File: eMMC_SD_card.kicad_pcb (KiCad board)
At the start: 4 copper layers, 24 x 20.3 mm, 29 parts, among them J1 SD_Card, U1 eMMC_5.1_BGA153

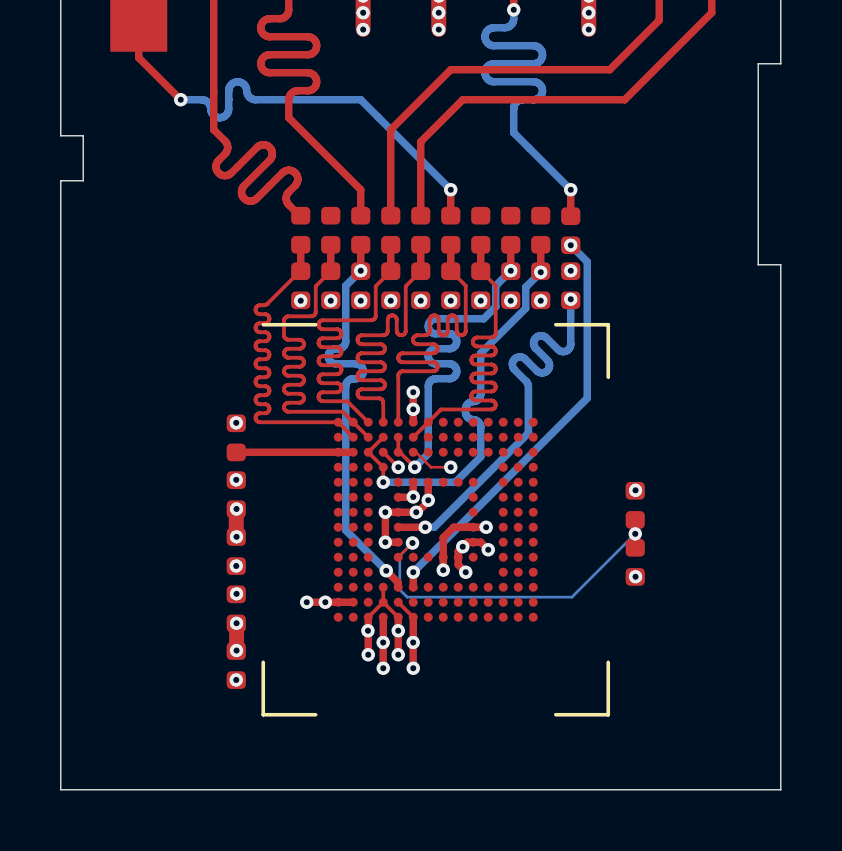
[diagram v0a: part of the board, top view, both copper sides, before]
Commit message: Introduce separate VCC and VCCq domains
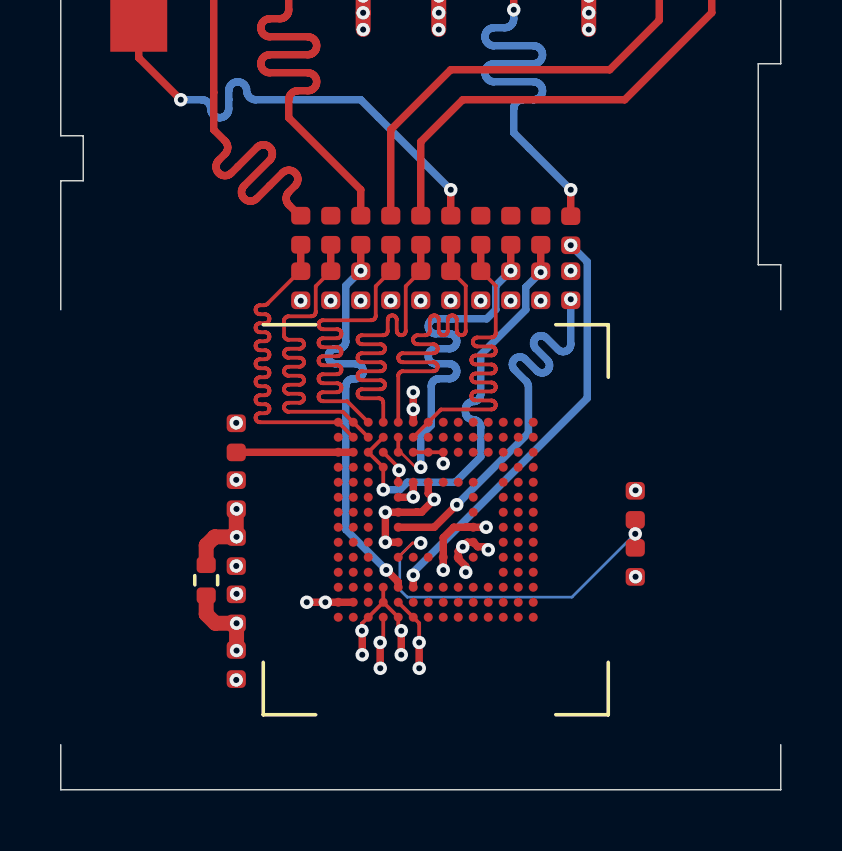
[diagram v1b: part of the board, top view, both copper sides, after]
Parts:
- added R22: 0R, Resistor_SMD:R_0402_1005Metric, F.Cu at (104.8, 125.0)
- moved C4 3.80 mm to (105.8, 124.1)
- moved C5 3.77 mm to (105.8, 127.8)
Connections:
- C5 pad 1: VCC -> VCCQ
- C6 pad 1: VCC -> VCCQ
- U1 pad C1: Net-(C2-Pad1) -> (no net)
- U1 pad C6: VCC -> VCCQ
- U1 pad C7: (no net) -> VCCQ
- U1 pad C8: (no net) -> VCCQ
- U1 pad M4: VCC -> VCCQ
- U1 pad N1: GND -> (no net)
- U1 pad N4: VCC -> VCCQ
- U1 pad P3: VCC -> VCCQ
- U1 pad P5: VCC -> VCCQ
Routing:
- net VCCQ: track 0.00 -> 8.67 mm, vias 0 -> 7
- net VCC: track 14.3 -> 9.29 mm, vias 26 -> 19
- net GND: track 21.1 -> 22.0 mm, vias 28 -> 27
- net Net-(C1-Pad2): track 12.2 -> 12.7 mm
- added copper zone on VCC, net VCCQ
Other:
- outline, holes or cut-outs redrawn

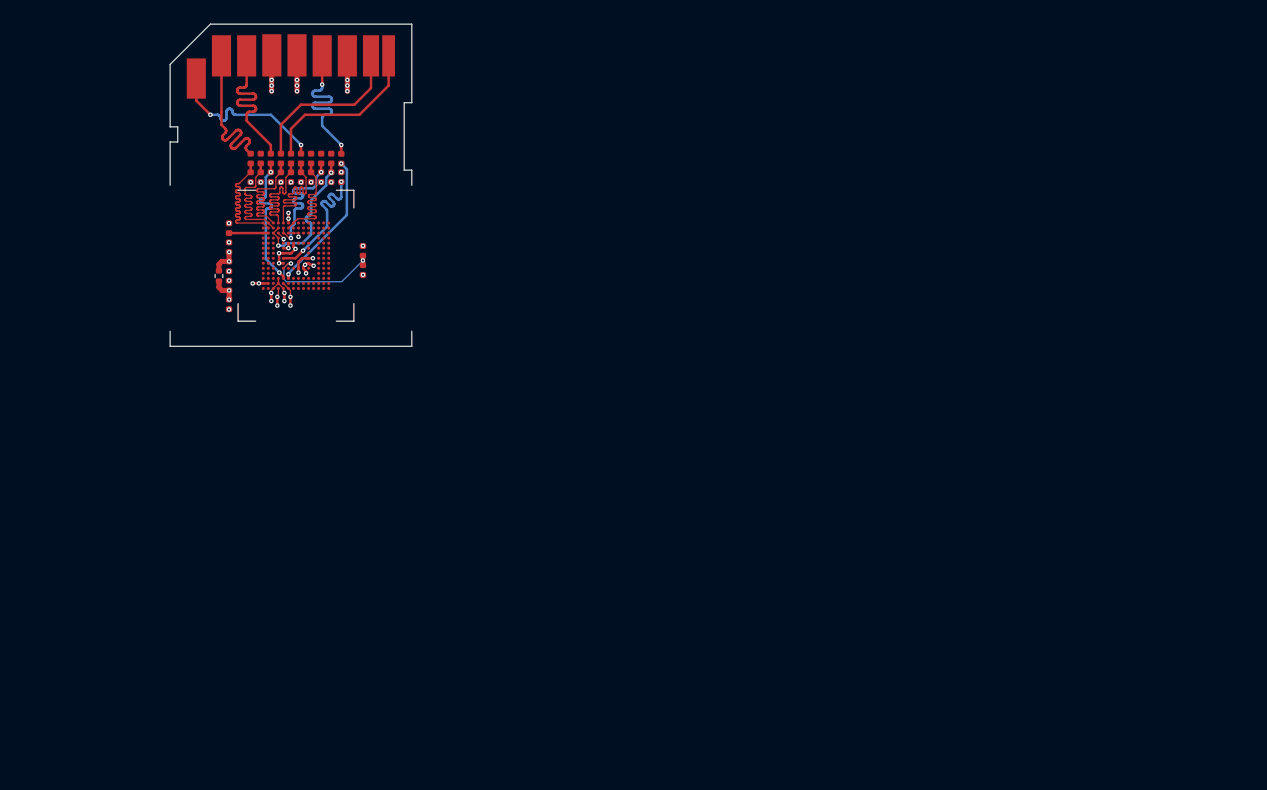
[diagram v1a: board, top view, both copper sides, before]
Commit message: Panelize
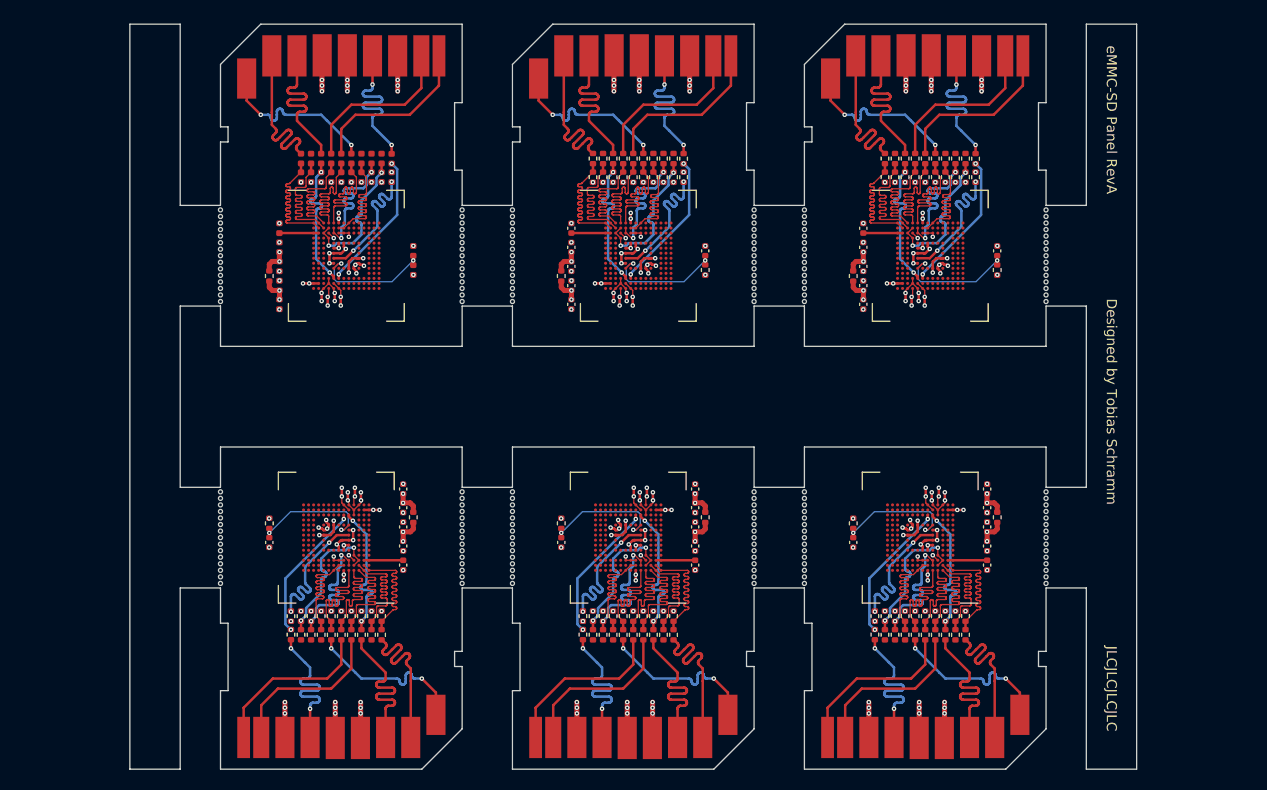
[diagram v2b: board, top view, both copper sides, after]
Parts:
- added C10: 4.7uF, Capacitor_SMD:C_0402_1005Metric, F.Cu at (139.8, 124.1)
- added C11: 4.7uF, Capacitor_SMD:C_0402_1005Metric, F.Cu at (139.8, 127.8)
- added C12: 100nF, Capacitor_SMD:C_0402_1005Metric, F.Cu at (139.8, 126.0)
- added C13: 100nF, Capacitor_SMD:C_0402_1005Metric, F.Cu at (182.2, 122.5)
- added C14: 100nF, Capacitor_SMD:C_0402_1005Metric, F.Cu at (168.8, 120.3)
- added C15: 100nF, Capacitor_SMD:C_0402_1005Metric, F.Cu at (168.8, 122.2)
- added C16: 4.7uF, Capacitor_SMD:C_0402_1005Metric, F.Cu at (168.8, 124.1)
- added C17: 4.7uF, Capacitor_SMD:C_0402_1005Metric, F.Cu at (168.8, 127.8)
- added C18: 100nF, Capacitor_SMD:C_0402_1005Metric, F.Cu at (168.8, 126.0)
- added C19: 100nF, Capacitor_SMD:C_0402_1005Metric, F.Cu at (109.8, 151.5)
- added C20: 100nF, Capacitor_SMD:C_0402_1005Metric, F.Cu at (123.2, 153.7)
- added C21: 100nF, Capacitor_SMD:C_0402_1005Metric, F.Cu at (123.2, 151.8)
- added C22: 4.7uF, Capacitor_SMD:C_0402_1005Metric, F.Cu at (123.2, 149.9)
- added C23: 4.7uF, Capacitor_SMD:C_0402_1005Metric, F.Cu at (123.2, 146.2)
- added C24: 100nF, Capacitor_SMD:C_0402_1005Metric, F.Cu at (123.2, 148.0)
- added C25: 100nF, Capacitor_SMD:C_0402_1005Metric, F.Cu at (138.8, 151.5)
- added C26: 100nF, Capacitor_SMD:C_0402_1005Metric, F.Cu at (152.2, 153.7)
- added C27: 100nF, Capacitor_SMD:C_0402_1005Metric, F.Cu at (152.2, 151.8)
- added C28: 4.7uF, Capacitor_SMD:C_0402_1005Metric, F.Cu at (152.2, 149.9)
- added C29: 4.7uF, Capacitor_SMD:C_0402_1005Metric, F.Cu at (152.2, 146.2)
- added C30: 100nF, Capacitor_SMD:C_0402_1005Metric, F.Cu at (152.2, 148.0)
- added C31: 100nF, Capacitor_SMD:C_0402_1005Metric, F.Cu at (167.8, 151.5)
- added C32: 100nF, Capacitor_SMD:C_0402_1005Metric, F.Cu at (181.2, 153.7)
- added C33: 100nF, Capacitor_SMD:C_0402_1005Metric, F.Cu at (181.2, 151.8)
- added C34: 4.7uF, Capacitor_SMD:C_0402_1005Metric, F.Cu at (181.2, 149.9)
- added C35: 4.7uF, Capacitor_SMD:C_0402_1005Metric, F.Cu at (181.2, 146.2)
- added C36: 100nF, Capacitor_SMD:C_0402_1005Metric, F.Cu at (181.2, 148.0)
- added C7: 100nF, Capacitor_SMD:C_0402_1005Metric, F.Cu at (153.2, 122.5)
- added C8: 100nF, Capacitor_SMD:C_0402_1005Metric, F.Cu at (139.8, 120.3)
- added C9: 100nF, Capacitor_SMD:C_0402_1005Metric, F.Cu at (139.8, 122.2)
- added H1: MountingHole, Perforation:Perforation_0.4mm, F.Cu at (105.0, 118.5)
- added H10: MountingHole, Perforation:Perforation_0.4mm, F.Cu at (105.0, 124.3)
- added H100: MountingHole, Perforation:Perforation_0.4mm, F.Cu at (105.0, 152.9)
- added H101: MountingHole, Perforation:Perforation_0.4mm, F.Cu at (129.0, 152.3)
- added H102: MountingHole, Perforation:Perforation_0.4mm, F.Cu at (129.0, 151.7)
- added H103: MountingHole, Perforation:Perforation_0.4mm, F.Cu at (129.0, 151.0)
- added H104: MountingHole, Perforation:Perforation_0.4mm, F.Cu at (129.0, 150.3)
- added H105: MountingHole, Perforation:Perforation_0.4mm, F.Cu at (129.0, 149.7)
- added H106: MountingHole, Perforation:Perforation_0.4mm, F.Cu at (105.0, 152.3)
- added H107: MountingHole, Perforation:Perforation_0.4mm, F.Cu at (105.0, 151.7)
- added H108: MountingHole, Perforation:Perforation_0.4mm, F.Cu at (105.0, 151.0)
- added H109: MountingHole, Perforation:Perforation_0.4mm, F.Cu at (105.0, 150.3)
- added H11: MountingHole, Perforation:Perforation_0.4mm, F.Cu at (105.0, 125.0)
- added H110: MountingHole, Perforation:Perforation_0.4mm, F.Cu at (105.0, 149.7)
- added H111: MountingHole, Perforation:Perforation_0.4mm, F.Cu at (129.0, 149.1)
- added H112: MountingHole, Perforation:Perforation_0.4mm, F.Cu at (129.0, 148.4)
- added H113: MountingHole, Perforation:Perforation_0.4mm, F.Cu at (129.0, 147.8)
- added H114: MountingHole, Perforation:Perforation_0.4mm, F.Cu at (129.0, 147.1)
- added H115: MountingHole, Perforation:Perforation_0.4mm, F.Cu at (129.0, 146.4)
- added H116: MountingHole, Perforation:Perforation_0.4mm, F.Cu at (105.0, 149.1)
- added H117: MountingHole, Perforation:Perforation_0.4mm, F.Cu at (105.0, 148.4)
- added H118: MountingHole, Perforation:Perforation_0.4mm, F.Cu at (105.0, 147.8)
- added H119: MountingHole, Perforation:Perforation_0.4mm, F.Cu at (105.0, 147.1)
- added H12: MountingHole, Perforation:Perforation_0.4mm, F.Cu at (105.0, 125.6)
- added H120: MountingHole, Perforation:Perforation_0.4mm, F.Cu at (105.0, 146.4)
- added H121: MountingHole, Perforation:Perforation_0.4mm, F.Cu at (158.0, 155.6)
- added H122: MountingHole, Perforation:Perforation_0.4mm, F.Cu at (158.0, 154.9)
- added H123: MountingHole, Perforation:Perforation_0.4mm, F.Cu at (158.0, 154.2)
- added H124: MountingHole, Perforation:Perforation_0.4mm, F.Cu at (158.0, 153.6)
- added H125: MountingHole, Perforation:Perforation_0.4mm, F.Cu at (158.0, 152.9)
- added H126: MountingHole, Perforation:Perforation_0.4mm, F.Cu at (134.0, 155.6)
- added H127: MountingHole, Perforation:Perforation_0.4mm, F.Cu at (134.0, 154.9)
- added H128: MountingHole, Perforation:Perforation_0.4mm, F.Cu at (134.0, 154.2)
- added H129: MountingHole, Perforation:Perforation_0.4mm, F.Cu at (134.0, 153.6)
- added H13: MountingHole, Perforation:Perforation_0.4mm, F.Cu at (105.0, 126.2)
- added H130: MountingHole, Perforation:Perforation_0.4mm, F.Cu at (134.0, 152.9)
- added H131: MountingHole, Perforation:Perforation_0.4mm, F.Cu at (158.0, 152.3)
- added H132: MountingHole, Perforation:Perforation_0.4mm, F.Cu at (158.0, 151.7)
- added H133: MountingHole, Perforation:Perforation_0.4mm, F.Cu at (158.0, 151.0)
- added H134: MountingHole, Perforation:Perforation_0.4mm, F.Cu at (158.0, 150.3)
- added H135: MountingHole, Perforation:Perforation_0.4mm, F.Cu at (158.0, 149.7)
- added H136: MountingHole, Perforation:Perforation_0.4mm, F.Cu at (134.0, 152.3)
- added H137: MountingHole, Perforation:Perforation_0.4mm, F.Cu at (134.0, 151.7)
- added H138: MountingHole, Perforation:Perforation_0.4mm, F.Cu at (134.0, 151.0)
- added H139: MountingHole, Perforation:Perforation_0.4mm, F.Cu at (134.0, 150.3)
- added H14: MountingHole, Perforation:Perforation_0.4mm, F.Cu at (105.0, 126.9)
- added H140: MountingHole, Perforation:Perforation_0.4mm, F.Cu at (134.0, 149.7)
- added H141: MountingHole, Perforation:Perforation_0.4mm, F.Cu at (158.0, 149.1)
- added H142: MountingHole, Perforation:Perforation_0.4mm, F.Cu at (158.0, 148.4)
- added H143: MountingHole, Perforation:Perforation_0.4mm, F.Cu at (158.0, 147.8)
- added H144: MountingHole, Perforation:Perforation_0.4mm, F.Cu at (158.0, 147.1)
- added H145: MountingHole, Perforation:Perforation_0.4mm, F.Cu at (158.0, 146.4)
- added H146: MountingHole, Perforation:Perforation_0.4mm, F.Cu at (134.0, 149.1)
- added H147: MountingHole, Perforation:Perforation_0.4mm, F.Cu at (134.0, 148.4)
- added H148: MountingHole, Perforation:Perforation_0.4mm, F.Cu at (134.0, 147.8)
- added H149: MountingHole, Perforation:Perforation_0.4mm, F.Cu at (134.0, 147.1)
- added H15: MountingHole, Perforation:Perforation_0.4mm, F.Cu at (105.0, 127.5)
- added H150: MountingHole, Perforation:Perforation_0.4mm, F.Cu at (134.0, 146.4)
- added H151: MountingHole, Perforation:Perforation_0.4mm, F.Cu at (187.0, 155.6)
- added H152: MountingHole, Perforation:Perforation_0.4mm, F.Cu at (187.0, 154.9)
- added H153: MountingHole, Perforation:Perforation_0.4mm, F.Cu at (187.0, 154.2)
- added H154: MountingHole, Perforation:Perforation_0.4mm, F.Cu at (187.0, 153.6)
- added H155: MountingHole, Perforation:Perforation_0.4mm, F.Cu at (187.0, 152.9)
- added H156: MountingHole, Perforation:Perforation_0.4mm, F.Cu at (163.0, 155.6)
- added H157: MountingHole, Perforation:Perforation_0.4mm, F.Cu at (163.0, 154.9)
- added H158: MountingHole, Perforation:Perforation_0.4mm, F.Cu at (163.0, 154.2)
- added H159: MountingHole, Perforation:Perforation_0.4mm, F.Cu at (163.0, 153.6)
- added H16: MountingHole, Perforation:Perforation_0.4mm, F.Cu at (129.0, 118.5)
- added H160: MountingHole, Perforation:Perforation_0.4mm, F.Cu at (163.0, 152.9)
- added H161: MountingHole, Perforation:Perforation_0.4mm, F.Cu at (187.0, 152.3)
- added H162: MountingHole, Perforation:Perforation_0.4mm, F.Cu at (187.0, 151.7)
- added H163: MountingHole, Perforation:Perforation_0.4mm, F.Cu at (187.0, 151.0)
- added H164: MountingHole, Perforation:Perforation_0.4mm, F.Cu at (187.0, 150.3)
- added H165: MountingHole, Perforation:Perforation_0.4mm, F.Cu at (187.0, 149.7)
- added H166: MountingHole, Perforation:Perforation_0.4mm, F.Cu at (163.0, 152.3)
- added H167: MountingHole, Perforation:Perforation_0.4mm, F.Cu at (163.0, 151.7)
- added H168: MountingHole, Perforation:Perforation_0.4mm, F.Cu at (163.0, 151.0)
- added H169: MountingHole, Perforation:Perforation_0.4mm, F.Cu at (163.0, 150.3)
- added H17: MountingHole, Perforation:Perforation_0.4mm, F.Cu at (129.0, 119.1)
- added H170: MountingHole, Perforation:Perforation_0.4mm, F.Cu at (163.0, 149.7)
- added H171: MountingHole, Perforation:Perforation_0.4mm, F.Cu at (187.0, 149.1)
- added H172: MountingHole, Perforation:Perforation_0.4mm, F.Cu at (187.0, 148.4)
- added H173: MountingHole, Perforation:Perforation_0.4mm, F.Cu at (187.0, 147.8)
- added H174: MountingHole, Perforation:Perforation_0.4mm, F.Cu at (187.0, 147.1)
- added H175: MountingHole, Perforation:Perforation_0.4mm, F.Cu at (187.0, 146.4)
- added H176: MountingHole, Perforation:Perforation_0.4mm, F.Cu at (163.0, 149.1)
- added H177: MountingHole, Perforation:Perforation_0.4mm, F.Cu at (163.0, 148.4)
- added H178: MountingHole, Perforation:Perforation_0.4mm, F.Cu at (163.0, 147.8)
- added H179: MountingHole, Perforation:Perforation_0.4mm, F.Cu at (163.0, 147.1)
- added H18: MountingHole, Perforation:Perforation_0.4mm, F.Cu at (129.0, 119.8)
- added H180: MountingHole, Perforation:Perforation_0.4mm, F.Cu at (163.0, 146.4)
- added H19: MountingHole, Perforation:Perforation_0.4mm, F.Cu at (129.0, 120.4)
- added H2: MountingHole, Perforation:Perforation_0.4mm, F.Cu at (105.0, 119.1)
- added H20: MountingHole, Perforation:Perforation_0.4mm, F.Cu at (129.0, 121.0)
- added H21: MountingHole, Perforation:Perforation_0.4mm, F.Cu at (129.0, 121.7)
- added H22: MountingHole, Perforation:Perforation_0.4mm, F.Cu at (129.0, 122.3)
- added H23: MountingHole, Perforation:Perforation_0.4mm, F.Cu at (129.0, 123.0)
- added H24: MountingHole, Perforation:Perforation_0.4mm, F.Cu at (129.0, 123.7)
- added H25: MountingHole, Perforation:Perforation_0.4mm, F.Cu at (129.0, 124.3)
- added H26: MountingHole, Perforation:Perforation_0.4mm, F.Cu at (129.0, 125.0)
- added H27: MountingHole, Perforation:Perforation_0.4mm, F.Cu at (129.0, 125.6)
- added H28: MountingHole, Perforation:Perforation_0.4mm, F.Cu at (129.0, 126.2)
- added H29: MountingHole, Perforation:Perforation_0.4mm, F.Cu at (129.0, 126.9)
- added H3: MountingHole, Perforation:Perforation_0.4mm, F.Cu at (105.0, 119.8)
- added H30: MountingHole, Perforation:Perforation_0.4mm, F.Cu at (129.0, 127.5)
- added H31: MountingHole, Perforation:Perforation_0.4mm, F.Cu at (134.0, 118.5)
- added H32: MountingHole, Perforation:Perforation_0.4mm, F.Cu at (134.0, 119.1)
- added H33: MountingHole, Perforation:Perforation_0.4mm, F.Cu at (134.0, 119.8)
- added H34: MountingHole, Perforation:Perforation_0.4mm, F.Cu at (134.0, 120.4)
- added H35: MountingHole, Perforation:Perforation_0.4mm, F.Cu at (134.0, 121.0)
- added H36: MountingHole, Perforation:Perforation_0.4mm, F.Cu at (158.0, 118.5)
- added H37: MountingHole, Perforation:Perforation_0.4mm, F.Cu at (158.0, 119.1)
- added H38: MountingHole, Perforation:Perforation_0.4mm, F.Cu at (158.0, 119.8)
- added H39: MountingHole, Perforation:Perforation_0.4mm, F.Cu at (158.0, 120.4)
- added H4: MountingHole, Perforation:Perforation_0.4mm, F.Cu at (105.0, 120.4)
- added H40: MountingHole, Perforation:Perforation_0.4mm, F.Cu at (158.0, 121.0)
- added H41: MountingHole, Perforation:Perforation_0.4mm, F.Cu at (134.0, 121.7)
- added H42: MountingHole, Perforation:Perforation_0.4mm, F.Cu at (134.0, 122.3)
- added H43: MountingHole, Perforation:Perforation_0.4mm, F.Cu at (134.0, 123.0)
- added H44: MountingHole, Perforation:Perforation_0.4mm, F.Cu at (134.0, 123.7)
- added H45: MountingHole, Perforation:Perforation_0.4mm, F.Cu at (134.0, 124.3)
- added H46: MountingHole, Perforation:Perforation_0.4mm, F.Cu at (158.0, 121.7)
- added H47: MountingHole, Perforation:Perforation_0.4mm, F.Cu at (158.0, 122.3)
- added H48: MountingHole, Perforation:Perforation_0.4mm, F.Cu at (158.0, 123.0)
- added H49: MountingHole, Perforation:Perforation_0.4mm, F.Cu at (158.0, 123.7)
- added H5: MountingHole, Perforation:Perforation_0.4mm, F.Cu at (105.0, 121.0)
- added H50: MountingHole, Perforation:Perforation_0.4mm, F.Cu at (158.0, 124.3)
- added H51: MountingHole, Perforation:Perforation_0.4mm, F.Cu at (134.0, 125.0)
- added H52: MountingHole, Perforation:Perforation_0.4mm, F.Cu at (134.0, 125.6)
- added H53: MountingHole, Perforation:Perforation_0.4mm, F.Cu at (134.0, 126.2)
- added H54: MountingHole, Perforation:Perforation_0.4mm, F.Cu at (134.0, 126.9)
- added H55: MountingHole, Perforation:Perforation_0.4mm, F.Cu at (134.0, 127.5)
- added H56: MountingHole, Perforation:Perforation_0.4mm, F.Cu at (158.0, 125.0)
- added H57: MountingHole, Perforation:Perforation_0.4mm, F.Cu at (158.0, 125.6)
- added H58: MountingHole, Perforation:Perforation_0.4mm, F.Cu at (158.0, 126.2)
- added H59: MountingHole, Perforation:Perforation_0.4mm, F.Cu at (158.0, 126.9)
- added H6: MountingHole, Perforation:Perforation_0.4mm, F.Cu at (105.0, 121.7)
- added H60: MountingHole, Perforation:Perforation_0.4mm, F.Cu at (158.0, 127.5)
- added H61: MountingHole, Perforation:Perforation_0.4mm, F.Cu at (163.0, 118.5)
- added H62: MountingHole, Perforation:Perforation_0.4mm, F.Cu at (163.0, 119.1)
- added H63: MountingHole, Perforation:Perforation_0.4mm, F.Cu at (163.0, 119.8)
- added H64: MountingHole, Perforation:Perforation_0.4mm, F.Cu at (163.0, 120.4)
- added H65: MountingHole, Perforation:Perforation_0.4mm, F.Cu at (163.0, 121.0)
- added H66: MountingHole, Perforation:Perforation_0.4mm, F.Cu at (187.0, 118.5)
- added H67: MountingHole, Perforation:Perforation_0.4mm, F.Cu at (187.0, 119.1)
- added H68: MountingHole, Perforation:Perforation_0.4mm, F.Cu at (187.0, 119.8)
- added H69: MountingHole, Perforation:Perforation_0.4mm, F.Cu at (187.0, 120.4)
- added H7: MountingHole, Perforation:Perforation_0.4mm, F.Cu at (105.0, 122.3)
- added H70: MountingHole, Perforation:Perforation_0.4mm, F.Cu at (187.0, 121.0)
- added H71: MountingHole, Perforation:Perforation_0.4mm, F.Cu at (163.0, 121.7)
- added H72: MountingHole, Perforation:Perforation_0.4mm, F.Cu at (163.0, 122.3)
- added H73: MountingHole, Perforation:Perforation_0.4mm, F.Cu at (163.0, 123.0)
- added H74: MountingHole, Perforation:Perforation_0.4mm, F.Cu at (163.0, 123.7)
- added H75: MountingHole, Perforation:Perforation_0.4mm, F.Cu at (163.0, 124.3)
- added H76: MountingHole, Perforation:Perforation_0.4mm, F.Cu at (187.0, 121.7)
- added H77: MountingHole, Perforation:Perforation_0.4mm, F.Cu at (187.0, 122.3)
- added H78: MountingHole, Perforation:Perforation_0.4mm, F.Cu at (187.0, 123.0)
- added H79: MountingHole, Perforation:Perforation_0.4mm, F.Cu at (187.0, 123.7)
- added H8: MountingHole, Perforation:Perforation_0.4mm, F.Cu at (105.0, 123.0)
- added H80: MountingHole, Perforation:Perforation_0.4mm, F.Cu at (187.0, 124.3)
- added H81: MountingHole, Perforation:Perforation_0.4mm, F.Cu at (163.0, 125.0)
- added H82: MountingHole, Perforation:Perforation_0.4mm, F.Cu at (163.0, 125.6)
- added H83: MountingHole, Perforation:Perforation_0.4mm, F.Cu at (163.0, 126.2)
- added H84: MountingHole, Perforation:Perforation_0.4mm, F.Cu at (163.0, 126.9)
- added H85: MountingHole, Perforation:Perforation_0.4mm, F.Cu at (163.0, 127.5)
- added H86: MountingHole, Perforation:Perforation_0.4mm, F.Cu at (187.0, 125.0)
- added H87: MountingHole, Perforation:Perforation_0.4mm, F.Cu at (187.0, 125.6)
- added H88: MountingHole, Perforation:Perforation_0.4mm, F.Cu at (187.0, 126.2)
- added H89: MountingHole, Perforation:Perforation_0.4mm, F.Cu at (187.0, 126.9)
- added H9: MountingHole, Perforation:Perforation_0.4mm, F.Cu at (105.0, 123.7)
- added H90: MountingHole, Perforation:Perforation_0.4mm, F.Cu at (187.0, 127.5)
- added H91: MountingHole, Perforation:Perforation_0.4mm, F.Cu at (129.0, 155.6)
- added H92: MountingHole, Perforation:Perforation_0.4mm, F.Cu at (129.0, 154.9)
- added H93: MountingHole, Perforation:Perforation_0.4mm, F.Cu at (129.0, 154.2)
- added H94: MountingHole, Perforation:Perforation_0.4mm, F.Cu at (129.0, 153.6)
- added H95: MountingHole, Perforation:Perforation_0.4mm, F.Cu at (129.0, 152.9)
- added H96: MountingHole, Perforation:Perforation_0.4mm, F.Cu at (105.0, 155.6)
- added H97: MountingHole, Perforation:Perforation_0.4mm, F.Cu at (105.0, 154.9)
- added H98: MountingHole, Perforation:Perforation_0.4mm, F.Cu at (105.0, 154.2)
- added H99: MountingHole, Perforation:Perforation_0.4mm, F.Cu at (105.0, 153.6)
- added J2: SD_Card, Connector_PCB_Edge_SD:SD, F.Cu at (134.0, 100.0)
- added J3: SD_Card, Connector_PCB_Edge_SD:SD, F.Cu at (163.0, 100.0)
- added J4: SD_Card, Connector_PCB_Edge_SD:SD, F.Cu at (129.0, 174.0)
- added J5: SD_Card, Connector_PCB_Edge_SD:SD, F.Cu at (158.0, 174.0)
- added J6: SD_Card, Connector_PCB_Edge_SD:SD, F.Cu at (187.0, 174.0)
- added R100: 10kR, Resistor_SMD:R_0402_1005Metric, F.Cu at (148.0, 158.8)
- added R101: 10kR, Resistor_SMD:R_0402_1005Metric, F.Cu at (144.0, 158.8)
- added R102: 10kR, Resistor_SMD:R_0402_1005Metric, F.Cu at (143.0, 158.8)
- added R103: 10kR, Resistor_SMD:R_0402_1005Metric, F.Cu at (142.0, 158.8)
- added R104: 10kR, Resistor_SMD:R_0402_1005Metric, F.Cu at (149.0, 158.8)
- added R105: 10kR, Resistor_SMD:R_0402_1005Metric, F.Cu at (150.0, 158.8)
- added R106: 10kR, Resistor_SMD:R_0402_1005Metric, F.Cu at (145.0, 158.8)
- added R107: 10kR, Resistor_SMD:R_0402_1005Metric, F.Cu at (146.0, 158.8)
- added R108: 10kR, Resistor_SMD:R_0402_1005Metric, F.Cu at (147.0, 158.8)
- added R109: 10kR, Resistor_SMD:R_0402_1005Metric, F.Cu at (141.0, 158.8)
- added R110: 0R, Resistor_SMD:R_0402_1005Metric, F.Cu at (153.2, 149.0)
- added R111: 33R, Resistor_SMD:R_0402_1005Metric, F.Cu at (174.0, 160.7)
- added R112: 33R, Resistor_SMD:R_0402_1005Metric, F.Cu at (171.0, 160.7)
- added R113: 33R, Resistor_SMD:R_0402_1005Metric, F.Cu at (177.0, 160.7)
- added R114: 33R, Resistor_SMD:R_0402_1005Metric, F.Cu at (175.0, 160.7)
- added R115: 33R, Resistor_SMD:R_0402_1005Metric, F.Cu at (178.0, 160.7)
- added R116: 33R, Resistor_SMD:R_0402_1005Metric, F.Cu at (173.0, 160.7)
- added R117: 33R, Resistor_SMD:R_0402_1005Metric, F.Cu at (176.0, 160.7)
- added R118: 33R, Resistor_SMD:R_0402_1005Metric, F.Cu at (179.0, 160.7)
- added R119: 33R, Resistor_SMD:R_0402_1005Metric, F.Cu at (172.0, 160.7)
- added R120: 33R, Resistor_SMD:R_0402_1005Metric, F.Cu at (170.0, 160.6)
- added R121: 10kR, Resistor_SMD:R_0402_1005Metric, F.Cu at (167.8, 149.6)
- added R122: 10kR, Resistor_SMD:R_0402_1005Metric, F.Cu at (177.0, 158.8)
- added R123: 10kR, Resistor_SMD:R_0402_1005Metric, F.Cu at (173.0, 158.8)
- added R124: 10kR, Resistor_SMD:R_0402_1005Metric, F.Cu at (172.0, 158.8)
- added R125: 10kR, Resistor_SMD:R_0402_1005Metric, F.Cu at (171.0, 158.8)
- added R126: 10kR, Resistor_SMD:R_0402_1005Metric, F.Cu at (178.0, 158.8)
- added R127: 10kR, Resistor_SMD:R_0402_1005Metric, F.Cu at (179.0, 158.8)
- added R128: 10kR, Resistor_SMD:R_0402_1005Metric, F.Cu at (174.0, 158.8)
- added R129: 10kR, Resistor_SMD:R_0402_1005Metric, F.Cu at (175.0, 158.8)
- added R130: 10kR, Resistor_SMD:R_0402_1005Metric, F.Cu at (176.0, 158.8)
- added R131: 10kR, Resistor_SMD:R_0402_1005Metric, F.Cu at (170.0, 158.8)
- added R132: 0R, Resistor_SMD:R_0402_1005Metric, F.Cu at (182.2, 149.0)
- added R23: 33R, Resistor_SMD:R_0402_1005Metric, F.Cu at (147.0, 113.3)
- added R24: 33R, Resistor_SMD:R_0402_1005Metric, F.Cu at (150.0, 113.3)
- added R25: 33R, Resistor_SMD:R_0402_1005Metric, F.Cu at (144.0, 113.3)
- added R26: 33R, Resistor_SMD:R_0402_1005Metric, F.Cu at (146.0, 113.3)
- added R27: 33R, Resistor_SMD:R_0402_1005Metric, F.Cu at (143.0, 113.3)
- added R28: 33R, Resistor_SMD:R_0402_1005Metric, F.Cu at (148.0, 113.3)
- added R29: 33R, Resistor_SMD:R_0402_1005Metric, F.Cu at (145.0, 113.3)
- added R30: 33R, Resistor_SMD:R_0402_1005Metric, F.Cu at (142.0, 113.3)
- added R31: 33R, Resistor_SMD:R_0402_1005Metric, F.Cu at (149.0, 113.3)
- added R32: 33R, Resistor_SMD:R_0402_1005Metric, F.Cu at (151.0, 113.4)
- added R33: 10kR, Resistor_SMD:R_0402_1005Metric, F.Cu at (153.2, 124.4)
- added R34: 10kR, Resistor_SMD:R_0402_1005Metric, F.Cu at (144.0, 115.2)
- added R35: 10kR, Resistor_SMD:R_0402_1005Metric, F.Cu at (148.0, 115.2)
- added R36: 10kR, Resistor_SMD:R_0402_1005Metric, F.Cu at (149.0, 115.2)
- added R37: 10kR, Resistor_SMD:R_0402_1005Metric, F.Cu at (150.0, 115.2)
- added R38: 10kR, Resistor_SMD:R_0402_1005Metric, F.Cu at (143.0, 115.2)
- added R39: 10kR, Resistor_SMD:R_0402_1005Metric, F.Cu at (142.0, 115.2)
- added R40: 10kR, Resistor_SMD:R_0402_1005Metric, F.Cu at (147.0, 115.2)
- added R41: 10kR, Resistor_SMD:R_0402_1005Metric, F.Cu at (146.0, 115.2)
- added R42: 10kR, Resistor_SMD:R_0402_1005Metric, F.Cu at (145.0, 115.2)
- added R43: 10kR, Resistor_SMD:R_0402_1005Metric, F.Cu at (151.0, 115.2)
- added R44: 0R, Resistor_SMD:R_0402_1005Metric, F.Cu at (138.8, 125.0)
- added R45: 33R, Resistor_SMD:R_0402_1005Metric, F.Cu at (176.0, 113.3)
- added R46: 33R, Resistor_SMD:R_0402_1005Metric, F.Cu at (179.0, 113.3)
- added R47: 33R, Resistor_SMD:R_0402_1005Metric, F.Cu at (173.0, 113.3)
- added R48: 33R, Resistor_SMD:R_0402_1005Metric, F.Cu at (175.0, 113.3)
- added R49: 33R, Resistor_SMD:R_0402_1005Metric, F.Cu at (172.0, 113.3)
- added R50: 33R, Resistor_SMD:R_0402_1005Metric, F.Cu at (177.0, 113.3)
- added R51: 33R, Resistor_SMD:R_0402_1005Metric, F.Cu at (174.0, 113.3)
- added R52: 33R, Resistor_SMD:R_0402_1005Metric, F.Cu at (171.0, 113.3)
- added R53: 33R, Resistor_SMD:R_0402_1005Metric, F.Cu at (178.0, 113.3)
- added R54: 33R, Resistor_SMD:R_0402_1005Metric, F.Cu at (180.0, 113.4)
- added R55: 10kR, Resistor_SMD:R_0402_1005Metric, F.Cu at (182.2, 124.4)
- added R56: 10kR, Resistor_SMD:R_0402_1005Metric, F.Cu at (173.0, 115.2)
- added R57: 10kR, Resistor_SMD:R_0402_1005Metric, F.Cu at (177.0, 115.2)
- added R58: 10kR, Resistor_SMD:R_0402_1005Metric, F.Cu at (178.0, 115.2)
- added R59: 10kR, Resistor_SMD:R_0402_1005Metric, F.Cu at (179.0, 115.2)
- added R60: 10kR, Resistor_SMD:R_0402_1005Metric, F.Cu at (172.0, 115.2)
- added R61: 10kR, Resistor_SMD:R_0402_1005Metric, F.Cu at (171.0, 115.2)
- added R62: 10kR, Resistor_SMD:R_0402_1005Metric, F.Cu at (176.0, 115.2)
- added R63: 10kR, Resistor_SMD:R_0402_1005Metric, F.Cu at (175.0, 115.2)
- added R64: 10kR, Resistor_SMD:R_0402_1005Metric, F.Cu at (174.0, 115.2)
- added R65: 10kR, Resistor_SMD:R_0402_1005Metric, F.Cu at (180.0, 115.2)
- added R66: 0R, Resistor_SMD:R_0402_1005Metric, F.Cu at (167.8, 125.0)
- added R67: 33R, Resistor_SMD:R_0402_1005Metric, F.Cu at (116.0, 160.7)
- added R68: 33R, Resistor_SMD:R_0402_1005Metric, F.Cu at (113.0, 160.7)
- added R69: 33R, Resistor_SMD:R_0402_1005Metric, F.Cu at (119.0, 160.7)
- added R70: 33R, Resistor_SMD:R_0402_1005Metric, F.Cu at (117.0, 160.7)
- added R71: 33R, Resistor_SMD:R_0402_1005Metric, F.Cu at (120.0, 160.7)
- added R72: 33R, Resistor_SMD:R_0402_1005Metric, F.Cu at (115.0, 160.7)
- added R73: 33R, Resistor_SMD:R_0402_1005Metric, F.Cu at (118.0, 160.7)
- added R74: 33R, Resistor_SMD:R_0402_1005Metric, F.Cu at (121.0, 160.7)
- added R75: 33R, Resistor_SMD:R_0402_1005Metric, F.Cu at (114.0, 160.7)
- added R76: 33R, Resistor_SMD:R_0402_1005Metric, F.Cu at (112.0, 160.6)
- added R77: 10kR, Resistor_SMD:R_0402_1005Metric, F.Cu at (109.8, 149.6)
- added R78: 10kR, Resistor_SMD:R_0402_1005Metric, F.Cu at (119.0, 158.8)
- added R79: 10kR, Resistor_SMD:R_0402_1005Metric, F.Cu at (115.0, 158.8)
- added R80: 10kR, Resistor_SMD:R_0402_1005Metric, F.Cu at (114.0, 158.8)
- added R81: 10kR, Resistor_SMD:R_0402_1005Metric, F.Cu at (113.0, 158.8)
- added R82: 10kR, Resistor_SMD:R_0402_1005Metric, F.Cu at (120.0, 158.8)
- added R83: 10kR, Resistor_SMD:R_0402_1005Metric, F.Cu at (121.0, 158.8)
- added R84: 10kR, Resistor_SMD:R_0402_1005Metric, F.Cu at (116.0, 158.8)
- added R85: 10kR, Resistor_SMD:R_0402_1005Metric, F.Cu at (117.0, 158.8)
- added R86: 10kR, Resistor_SMD:R_0402_1005Metric, F.Cu at (118.0, 158.8)
- added R87: 10kR, Resistor_SMD:R_0402_1005Metric, F.Cu at (112.0, 158.8)
- added R88: 0R, Resistor_SMD:R_0402_1005Metric, F.Cu at (124.2, 149.0)
- added R89: 33R, Resistor_SMD:R_0402_1005Metric, F.Cu at (145.0, 160.7)
- added R90: 33R, Resistor_SMD:R_0402_1005Metric, F.Cu at (142.0, 160.7)
- added R91: 33R, Resistor_SMD:R_0402_1005Metric, F.Cu at (148.0, 160.7)
- added R92: 33R, Resistor_SMD:R_0402_1005Metric, F.Cu at (146.0, 160.7)
- added R93: 33R, Resistor_SMD:R_0402_1005Metric, F.Cu at (149.0, 160.7)
- added R94: 33R, Resistor_SMD:R_0402_1005Metric, F.Cu at (144.0, 160.7)
- added R95: 33R, Resistor_SMD:R_0402_1005Metric, F.Cu at (147.0, 160.7)
- added R96: 33R, Resistor_SMD:R_0402_1005Metric, F.Cu at (150.0, 160.7)
- added R97: 33R, Resistor_SMD:R_0402_1005Metric, F.Cu at (143.0, 160.7)
- added R98: 33R, Resistor_SMD:R_0402_1005Metric, F.Cu at (141.0, 160.6)
- added R99: 10kR, Resistor_SMD:R_0402_1005Metric, F.Cu at (138.8, 149.6)
- added U2: eMMC_5.1_BGA153, Package_BGA_eMMC:eMMC-FBGA-153, F.Cu at (146.5, 123.0)
- added U3: eMMC_5.1_BGA153, Package_BGA_eMMC:eMMC-FBGA-153, F.Cu at (175.5, 123.0)
- added U4: eMMC_5.1_BGA153, Package_BGA_eMMC:eMMC-FBGA-153, F.Cu at (116.5, 151.0)
- added U5: eMMC_5.1_BGA153, Package_BGA_eMMC:eMMC-FBGA-153, F.Cu at (145.5, 151.0)
- added U6: eMMC_5.1_BGA153, Package_BGA_eMMC:eMMC-FBGA-153, F.Cu at (174.5, 151.0)
- moved C1 5.00 mm to (124.2, 122.5)
- moved C2 5.00 mm to (110.8, 120.3)
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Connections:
- U1 pad A7: /Adapter 1/D7 -> Net-(U1-PadA7)
- U1 pad A8: (no net) -> /Adapter 1/D7
- U1 pad B7: (no net) -> /Adapter 1/D7
- U1 pad C7: VCCQ -> (no net)
- U1 pad C8: VCCQ -> (no net)
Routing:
- net GND: track 22.0 -> 128.9 mm, vias 27 -> 162
- net (no net): track 0.00 -> 56.4 mm
- net VCC: track 9.29 -> 55.8 mm, vias 19 -> 114
- net VCCQ: track 8.67 -> 52.0 mm, vias 7 -> 42
- net /Adapter 3/DAT2: track 0.00 -> 16.9 mm, vias 0 -> 2
- net /Adapter 2/DAT2: track 0.00 -> 16.9 mm, vias 0 -> 2
- net /Adapter 6/DAT2: track 0.00 -> 16.9 mm, vias 0 -> 2
- net /Adapter 5/DAT2: track 0.00 -> 16.9 mm, vias 0 -> 2
- net /Adapter 4/DAT2: track 0.00 -> 16.9 mm, vias 0 -> 2
- net /Adapter 3/CMD: track 0.00 -> 16.9 mm
- net /Adapter 2/CMD: track 0.00 -> 16.9 mm
- net /Adapter 6/CMD: track 0.00 -> 16.9 mm
- net /Adapter 5/CMD: track 0.00 -> 16.9 mm
- net /Adapter 4/CMD: track 0.00 -> 16.9 mm
- net /Adapter 4/CLK: track 0.00 -> 16.9 mm, vias 0 -> 2
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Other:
- board size 24 x 20.3 mm -> 100 x 74 mm
- board text added: "8GB"
- board text added: "Designed by Tobias Schramm"
- board text added: "JLCJLCJLCJLC"
- board text added: "by Tobias Schramm"
- board text added: "eMMC-SD"
- board text added: "eMMC-SD Panel RevA"

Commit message: Add tooling holes
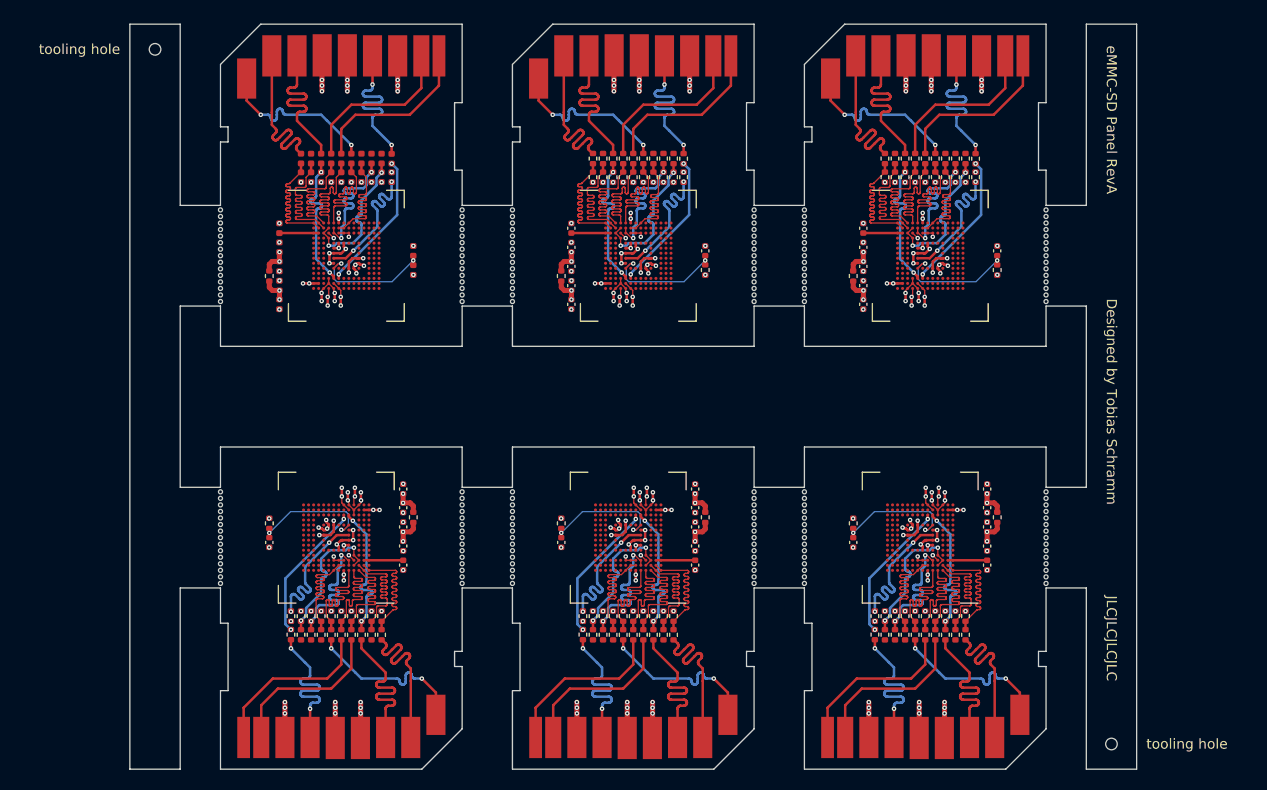
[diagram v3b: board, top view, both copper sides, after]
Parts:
- added H181: MountingHole, ToolingHole:ToolingHole_JLCSMT, F.Cu at (98.5, 102.5)
- added H182: MountingHole, ToolingHole:ToolingHole_JLCSMT, F.Cu at (193.5, 171.5)
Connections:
- U1 pad A8: /Adapter 1/D7 -> (no net)
- U1 pad B7: /Adapter 1/D7 -> (no net)
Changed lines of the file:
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@@
     (tracks 9810)
     (zones 0)
-    (modules 360)
+    (modules 362)
     (nets 154)
   )
@@
     (add_net VCCQ)
   )
+  (module ToolingHole:ToolingHole_JLCSMT (layer F.Cu)
+    (at 193.5 171.5)
+    (fp_text reference H182 (at 0 0.5) (layer F.SilkS) hide
+      (effects (font (size 1 1) (thickness 0.15)))
+    )
+    (fp_text value MountingHole (at 0 -0.5) (layer F.Fab)
+      (effects (font (size 1 1) (thickness 0.15)))
+    )
+    (fp_text user "tooling hole" (at 7.5 0) (layer F.SilkS)
+      (effects (font (size 1 1) (thickness 0.15)))
+    )
+    (pad "" np_thru_hole circle (at 0 0) (size 1.152 1.152) (drill 1.152) (layers *.Cu *.Mask))
+  )
+  (module ToolingHole:ToolingHole_JLCSMT (layer F.Cu)
+    (at 98.5 102.5)
+    (fp_text reference H181 (at 0 0.5) (layer F.SilkS) hide
+      (effects (font (size 1 1) (thickness 0.15)))
+    )
+    (fp_text value MountingHole (at 0 -0.5) (layer F.Fab)
+      (effects (font (size 1 1) (thickness 0.15)))
+    )
+    (fp_text user "tooling hole" (at -7.5 0) (layer F.SilkS)
+      (effects (font (size 1 1) (thickness 0.15)))
+    )
+    (pad "" np_thru_hole circle (at 0 0) (size 1.152 1.152) (drill 1.152) (layers *.Cu *.Mask))
+  )
   (module Package_BGA_eMMC:eMMC-FBGA-153 (layer F.Cu)
     (at 174.5 151 180)
@@
     (pad C8 smd circle (at 0.25 -2.25) (size 0.3 0.3) (layers F.Cu F.Paste F.Mask))
     (pad B8 smd circle (at 0.25 -2.75) (size 0.3 0.3) (layers F.Cu F.Paste F.Mask))
-    (pad A8 smd circle (at 0.25 -3.25) (size 0.3 0.3) (layers F.Cu F.Paste F.Mask)
-      (net 19 "/Adapter 1/D7"))
+    (pad A8 smd circle (at 0.25 -3.25) (size 0.3 0.3) (layers F.Cu F.Paste F.Mask))
     (pad P7 smd circle (at -0.25 3.25) (size 0.3 0.3) (layers F.Cu F.Paste F.Mask))
     (pad N7 smd circle (at -0.25 2.75) (size 0.3 0.3) (layers F.Cu F.Paste F.Mask))
@@
       (net 2 GND))
     (pad C7 smd circle (at -0.25 -2.25) (size 0.3 0.3) (layers F.Cu F.Paste F.Mask))
-    (pad B7 smd circle (at -0.25 -2.75) (size 0.3 0.3) (layers F.Cu F.Paste F.Mask)
-      (net 19 "/Adapter 1/D7"))
+    (pad B7 smd circle (at -0.25 -2.75) (size 0.3 0.3) (layers F.Cu F.Paste F.Mask))
     (pad A7 smd circle (at -0.25 -3.25) (size 0.3 0.3) (layers F.Cu F.Paste F.Mask)
       (net 143 "Net-(U1-PadA7)"))
@@
     (effects (font (size 1 1) (thickness 0.15)))
   )
-  (gr_text JLCJLCJLCJLC (at 193.5 166 270) (layer F.SilkS)
+  (gr_text JLCJLCJLCJLC (at 193.5 161 270) (layer F.SilkS)
     (effects (font (size 1 1) (thickness 0.15)))
   )

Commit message: Set SD lock to unprotected
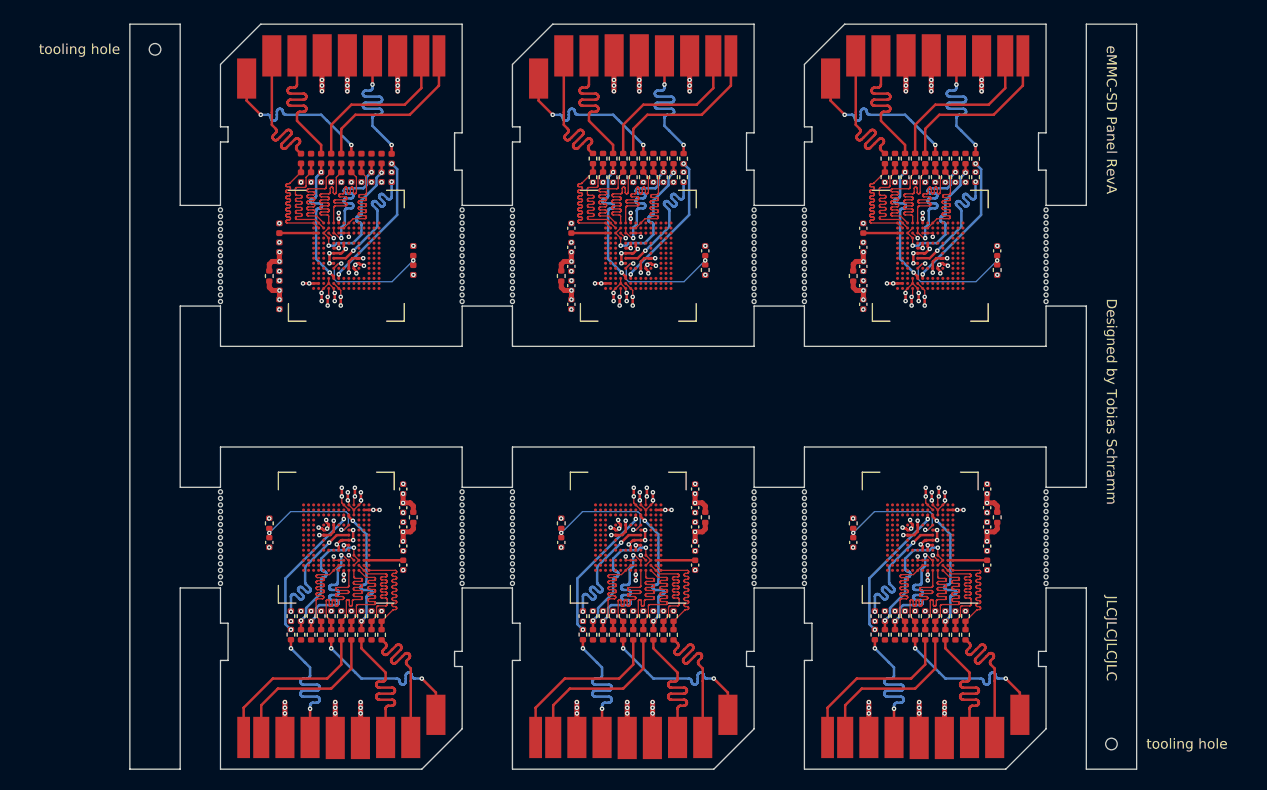
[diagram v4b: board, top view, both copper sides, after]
